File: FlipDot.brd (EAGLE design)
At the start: 97.8 x 70.8 mm, 96 parts, among them X1 FAC64S

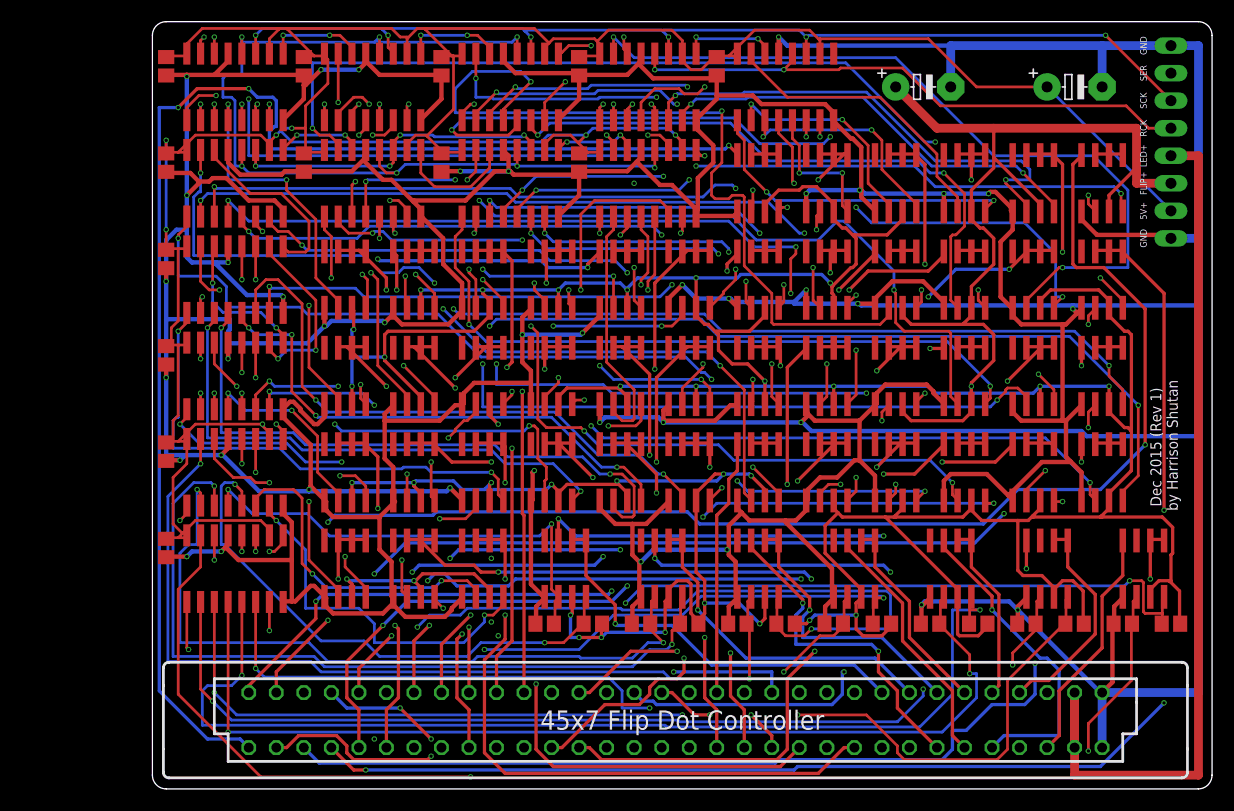
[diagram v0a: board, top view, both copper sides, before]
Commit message: Initial HW Rev2 commit.
This Rev is a work in progress and is not ready to be sent to fab.
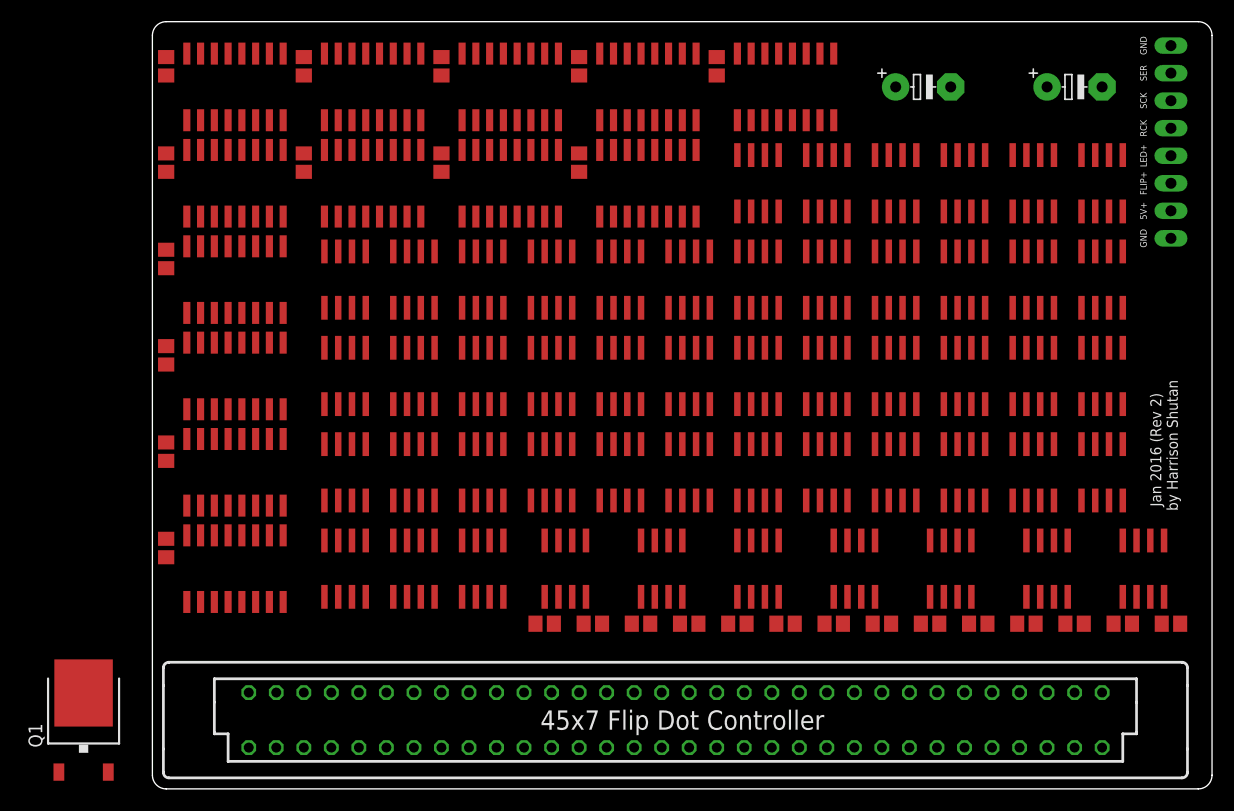
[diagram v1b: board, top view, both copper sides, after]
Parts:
- added Q1: FDD4141TO252, transistor-fet:TO252
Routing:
- net GND: track 958.2 -> 0.00 mm, vias 39 -> 0
- net FLIPVOLTPOSITIVE: track 563.4 -> 0.00 mm, vias 34 -> 0
- net VCC: track 314.8 -> 0.00 mm, vias 9 -> 0
- net RCK: track 210.5 -> 0.00 mm, vias 13 -> 0
- net SCK: track 199.2 -> 0.00 mm, vias 15 -> 0
- net MAINSERIALLINE: track 146.2 -> 0.00 mm, vias 1 -> 0
- net COL40COMMON: track 130.1 -> 0.00 mm, vias 2 -> 0
- net COLPGATE14: track 129.6 -> 0.00 mm, vias 2 -> 0
- net COL41COMMON: track 128.7 -> 0.00 mm, vias 2 -> 0
- net COL45COMMON: track 127.6 -> 0.00 mm, vias 3 -> 0
- net COL39COMMON: track 126.3 -> 0.00 mm, vias 3 -> 0
- net ROWNGATE1: track 120.3 -> 0.00 mm, vias 2 -> 0
- net COL42COMMON: track 119.7 -> 0.00 mm, vias 4 -> 0
- net COL43COMMON: track 114.9 -> 0.00 mm, vias 2 -> 0
- net COLNGATE14: track 111.9 -> 0.00 mm, vias 3 -> 0
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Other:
- board text added: "Jan 2016 (Rev 2) by Harrison Shutan"
- board text removed: "Dec 2015 (Rev 1) by Harrison Shutan"
